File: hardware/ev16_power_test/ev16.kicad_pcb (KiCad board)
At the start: 4 copper layers, 125 x 80 mm, 172 parts, among them CN1 Conn_05x02_Female, CN2 PJ-242, J1 USB_C_Receptacle, J10 Conn_01x03_Pin, J11 Conn_02x05_Counter_Clockwise, J2 Conn_01x02_Socket, J3 AudioJack4, J4 Conn_02x03_Odd_Even, J5 Conn_02x03_Odd_Even, J6 Conn_02x05_Counter_Clockwise, J7 Conn_02x05_Counter_Clockwise, J8 Conn_02x05_Counter_Clockwise, J9 Conn_02x05_Counter_Clockwise, Q1 2N7002, Q2 2N7002, Q3 2N7002, SW1 SW_SPDT, SW2 SW_Push, SW3 SW_Push, SW4 SW_Push, SW5 SW_Push, SW6 SW_Push, SW7 SW_Push, U1 BQ21040DBV, U10 STM32F405RGTx, U2 USBLC6-2P6, U3 STM32F072CBTx, U4 CH340C, U5 TPS63060, U6 WM8960CGEFL/RV, U7 ESP32-S3-WROOM-1, U8 M24C02-RMN6TP, Y1 Crystal_GND24

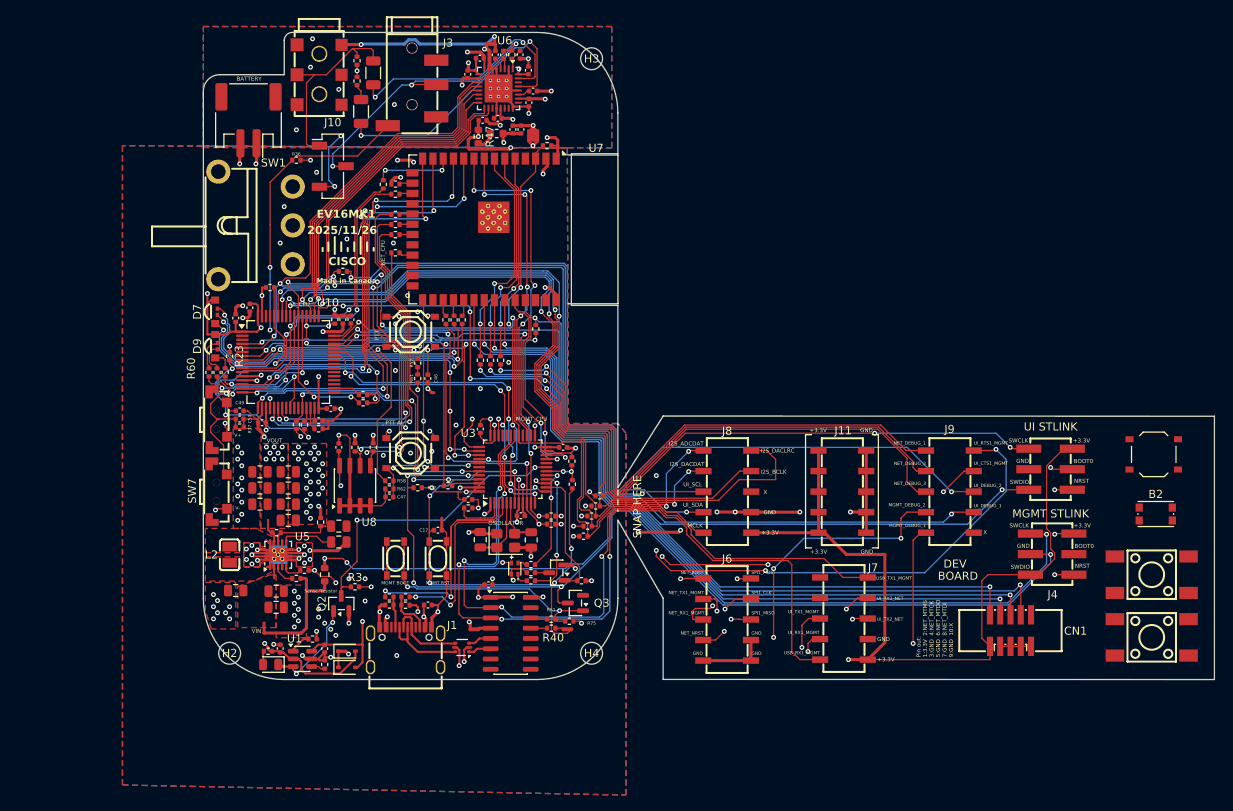
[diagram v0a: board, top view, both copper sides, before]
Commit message: New linear regulator, ideal diodes, began working on the layout
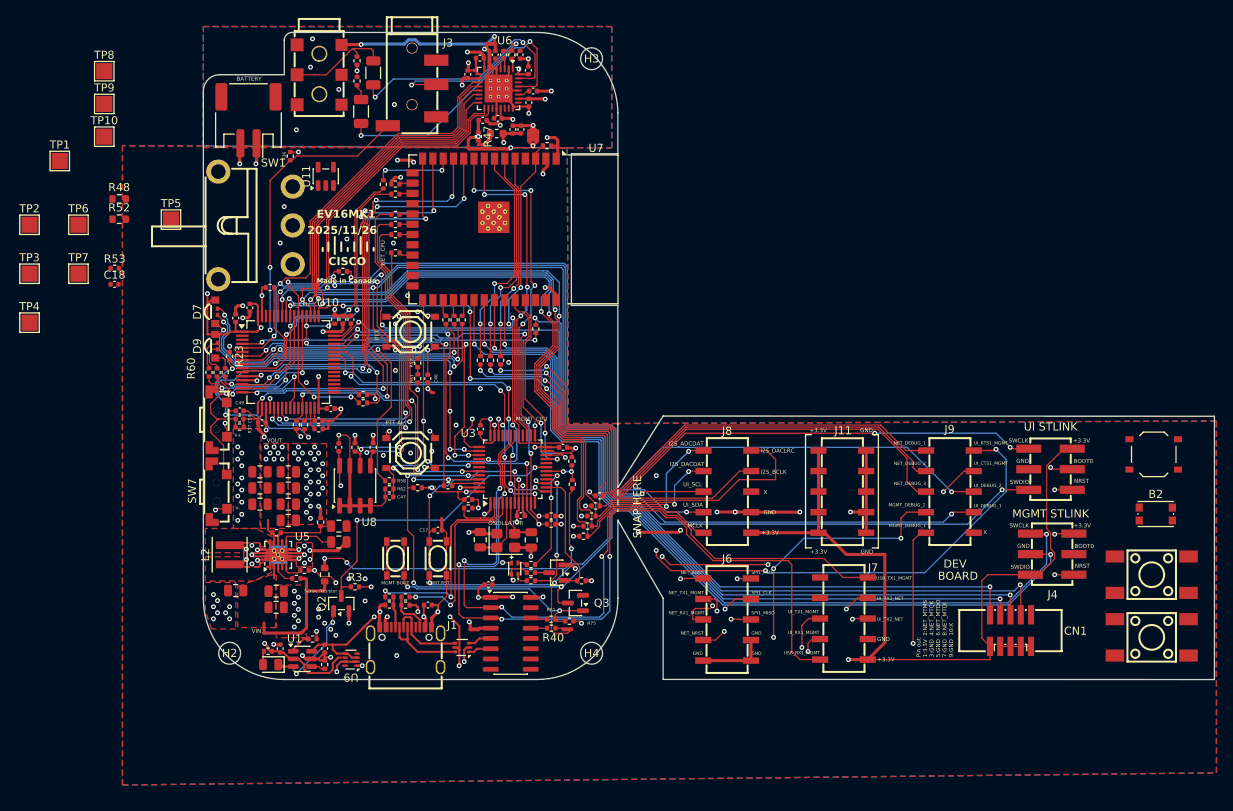
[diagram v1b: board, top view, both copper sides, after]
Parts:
- removed D2, D3: 1N5819WS, Diode_SMD:D_SOD-323
- removed J10: Conn_01x03_Pin, Connector_PinSocket_2.54mm:PinSocket_1x03_P2.54mm_Vertical_SMD_Pin1Left
- added C18: 1u, Capacitor_SMD:C_0402_1005Metric, F.Cu at (39.0, 61.1)
- added R48: 0R1, Resistor_SMD:R_0603_1608Metric, F.Cu at (39.6, 50.6)
- added R52: 0R1, Resistor_SMD:R_0603_1608Metric, F.Cu at (39.6, 53.1)
- added R53: 15k, Resistor_SMD:R_0402_1005Metric, F.Cu at (39.0, 59.2)
- added TP1: TestPoint, TestPoint:TestPoint_Pad_2.0x2.0mm, F.Cu at (32.2, 45.9)
- added TP10: TestPoint, TestPoint:TestPoint_Pad_2.0x2.0mm, F.Cu at (37.8, 42.9)
- added TP2: TestPoint, TestPoint:TestPoint_Pad_2.0x2.0mm, F.Cu at (28.5, 53.8)
- added TP3: TestPoint, TestPoint:TestPoint_Pad_2.0x2.0mm, F.Cu at (28.5, 59.8)
- added TP4: TestPoint, TestPoint:TestPoint_Pad_2.0x2.0mm, F.Cu at (28.5, 65.9)
- added TP5: TestPoint, TestPoint:TestPoint_Pad_2.0x2.0mm, F.Cu at (46.0, 53.1)
- added TP6: TestPoint, TestPoint:TestPoint_Pad_2.0x2.0mm, F.Cu at (34.6, 53.8)
- added TP7: TestPoint, TestPoint:TestPoint_Pad_2.0x2.0mm, F.Cu at (34.6, 59.8)
- added TP8: TestPoint, TestPoint:TestPoint_Pad_2.0x2.0mm, F.Cu at (37.8, 34.8)
- added TP9: TestPoint, TestPoint:TestPoint_Pad_2.0x2.0mm, F.Cu at (37.8, 38.8)
- added U11: ME6211C28M5, Package_TO_SOT_SMD:SOT-23-5, F.Cu at (65.1, 47.8)
- added U9: TPS2116DRL, Package_TO_SOT_SMD:SOT-583-8, F.Cu at (68.3, 107.5)
- L2: value 1uH -> 1.5uH; footprint Hactar_Footprints:MCL2016A1R0MT -> Inductor_SMD:L_Coilcraft_XxL4020
- R47: value 0R1 -> 10k; footprint Resistor_SMD:R_0603_1608Metric -> Resistor_SMD:R_0402_1005Metric
- moved R36 0.90 mm to (60.8, 45.3), turned to 90 degrees
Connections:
- C10 pad 1: +3.3VA -> Net-(C10-Pad1)
- C11 pad 1: +3.3VA -> Net-(C10-Pad1)
- C22 pad 1: +3.3V -> Net-(U5-VOUT)
- C24 pad 1: +3.3V -> Net-(U5-VOUT)
- C27 pad 1: +3.3V -> Net-(U5-VOUT)
- C29 pad 1: +3.3V -> Net-(U5-VOUT)
- C30 pad 1: +3.3V -> Net-(U5-VOUT)
- C31 pad 1: +3.3V -> Net-(U5-VOUT)
- C35 pad 1: +3.3V -> Net-(U5-VOUT)
- L1 pad 1: Net-(L1-Pad1) -> Net-(U11-V_{OUT})
- L1 pad 2: +3.3VA -> Net-(C10-Pad1)
- R12 pad 2: Net-(SW1-C) -> VSYS
- R14 pad 1: Net-(SW1-C) -> VSYS
- R26 pad 2: +3.3V -> Net-(U5-VOUT)
- R28 pad 2: +3.3V -> Net-(U5-VOUT)
- R47 pad 1: +3.3V -> GND
- R47 pad 2: Net-(L1-Pad1) -> Net-(U9-PR1)
- SW1 pad 2: Net-(D2-K) -> VSYS
- U5 pad 9: +3.3V -> Net-(U5-VOUT)
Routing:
- net VSYS: track 0.00 -> 102.3 mm, vias 0 -> 3
- net Net-(D2-K): track 64.7 -> 0.00 mm, vias 1 -> 0
- net Net-(SW1-C): track 94.2 -> 73.5 mm, vias 3 -> 1
- net /MIC_P: track 36.2 -> 19.7 mm, vias 3 -> 2
- net /HP_L: track 23.8 -> 13.1 mm
- net GNDA: track 86.0 -> 76.9 mm, vias 13 -> 11
- net +3.3V: track 296.4 -> 287.9 mm, vias 47 -> 37
- net Net-(U5-VOUT): track 0.00 -> 7.36 mm, vias 0 -> 10
- net VBUS: track 37.8 -> 34.5 mm, vias 4 -> 5
- net Net-(U11-V_{OUT}): track 0.00 -> 2.39 mm
- net Net-(L1-Pad1): track 2.39 -> 0.00 mm
- net Net-(J2-Pin_2): track 79.5 -> 77.6 mm
- net GND: track 312.3 -> 313.0 mm
- added copper zone on F.Cu, net Net-(U5-VOUT)
- removed copper zone on F.Cu, net +3.3V

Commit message: finished laying out the board with the power changes
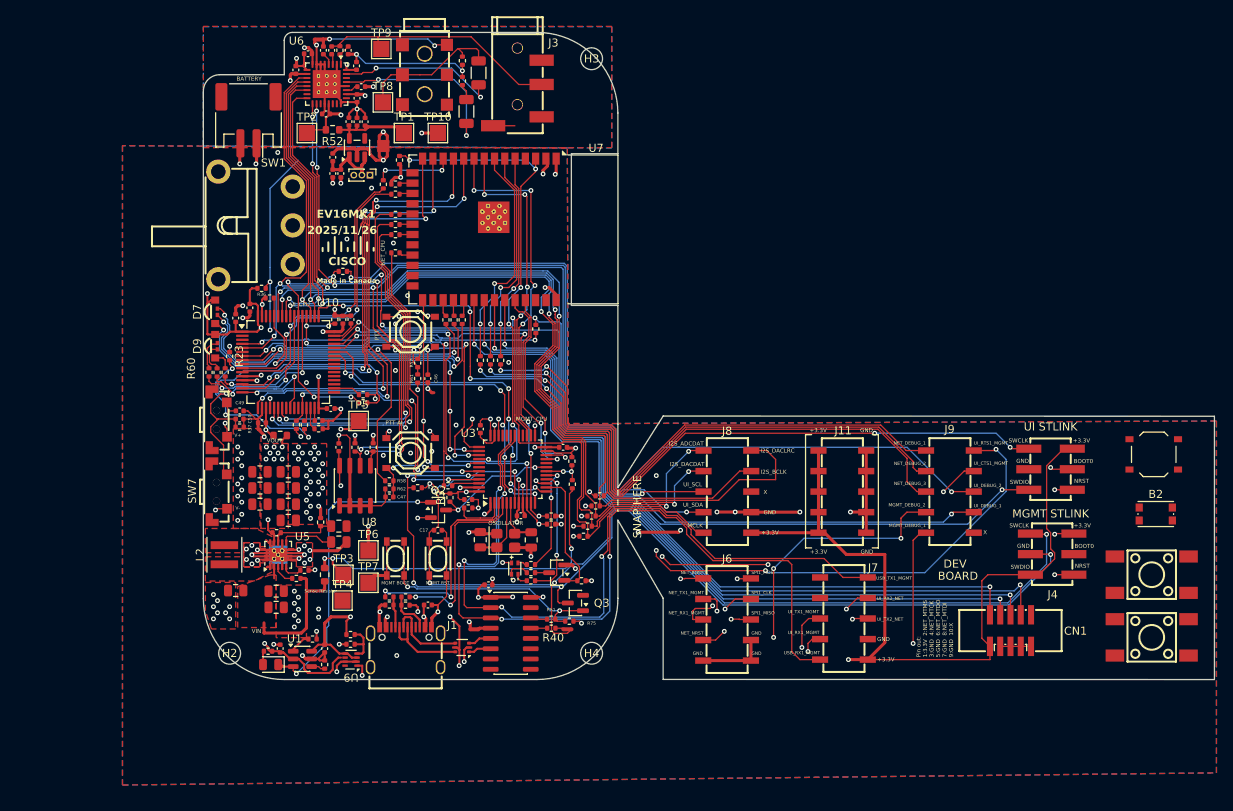
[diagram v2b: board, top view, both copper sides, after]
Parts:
- removed L1: 120Ω, Inductor_SMD:L_0603_1608Metric
- added C51: 100n, Capacitor_SMD:C_0402_1005Metric, F.Cu at (66.0, 47.4)
- added C52: 100n, Capacitor_SMD:C_0402_1005Metric, F.Cu at (66.0, 45.4)
- added J10: Conn_01x03_Pin, Connector_PinHeader_1.00mm:PinHeader_1x03_P1.00mm_Vertical, F.Cu at (70.6, 47.6)
- C10: value 1u -> 100n
- C11: value 10n -> 100n
- C24, C27, C29, C30, C31, C35: value 10u -> 22u
- moved R47 64.7 mm to (68.2, 105.6), turned to 0 degrees
- moved TP6 53.9 mm to (70.4, 94.0)
- moved R53 53.9 mm to (68.2, 104.4), turned to 180 degrees
- moved TP3 53.8 mm to (67.3, 97.1)
- moved TP7 52.4 mm to (70.4, 98.0)
- moved TP4 51.7 mm to (67.2, 100.2)
- moved TP1 42.7 mm to (74.8, 42.4)
- moved TP10 41.3 mm to (79.0, 42.4)
- moved TP2 36.1 mm to (62.8, 42.4)
- moved R48 35.4 mm to (59.5, 79.8), turned to 180 degrees
- moved C18 35.3 mm to (68.0, 41.0), turned to 90 degrees
- moved TP9 34.9 mm to (72.0, 32.0)
- moved TP8 34.7 mm to (72.2, 38.6)
- moved TP5 34.0 mm to (69.2, 78.0)
- moved R52 28.6 mm to (66.0, 42.0), turned to 180 degrees
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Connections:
- C10 pad 1: Net-(C10-Pad1) -> Net-(U11-V_{OUT})
- C11 pad 1: Net-(C10-Pad1) -> Net-(U11-V_{OUT})
- C18 pad 2: GND -> GNDA
- C7 pad 1: +3.3V -> Net-(J10-Pin_2)
- R52 pad 1: Net-(C10-Pad1) -> Net-(U11-V_{OUT})
- TP1 pad 1: Net-(C10-Pad1) -> Net-(U11-V_{OUT})
- U10 pad 13: +3.3VA -> +3.3V
- U11 pad 1: +3.3V -> Net-(J10-Pin_2)
- U11 pad 3: +3.3V -> Net-(J10-Pin_2)
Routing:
- net +3.3VA: track 80.6 -> 21.9 mm, vias 5 -> 3
- net GNDA: track 76.9 -> 103.5 mm, vias 11 -> 7
- net Net-(D1-K): track 12.7 -> 38.0 mm
- net /CHG_FB: track 37.6 -> 16.0 mm
- net Net-(U5-VOUT): track 7.36 -> 26.1 mm, vias 10 -> 11
- net /NET_NRST: track 97.6 -> 113.1 mm, vias 5 -> 7
- net VSYS: track 102.3 -> 117.0 mm
- net Net-(U6-HP_R): track 35.3 -> 22.5 mm
- net /UI_SDA1: track 153.0 -> 141.3 mm, vias 6 -> 8
- net /UI_SCL1: track 147.8 -> 136.5 mm, vias 6 -> 8
- net /MIC_P: track 19.7 -> 30.7 mm, vias 2 -> 0
- net /I2S_BCLK: track 130.2 -> 119.7 mm
- net Net-(U6-HP_L): track 30.4 -> 20.0 mm
- net GND: track 313.0 -> 302.8 mm, vias 144 -> 137
- net /MCLK: track 143.1 -> 133.0 mm
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- added copper zone on In2.Cu, net +3.3VA
- removed copper zone on B.Cu, net GNDA
- removed copper zone on F.Cu, net GNDA
- removed copper zone on In2.Cu, net GNDA

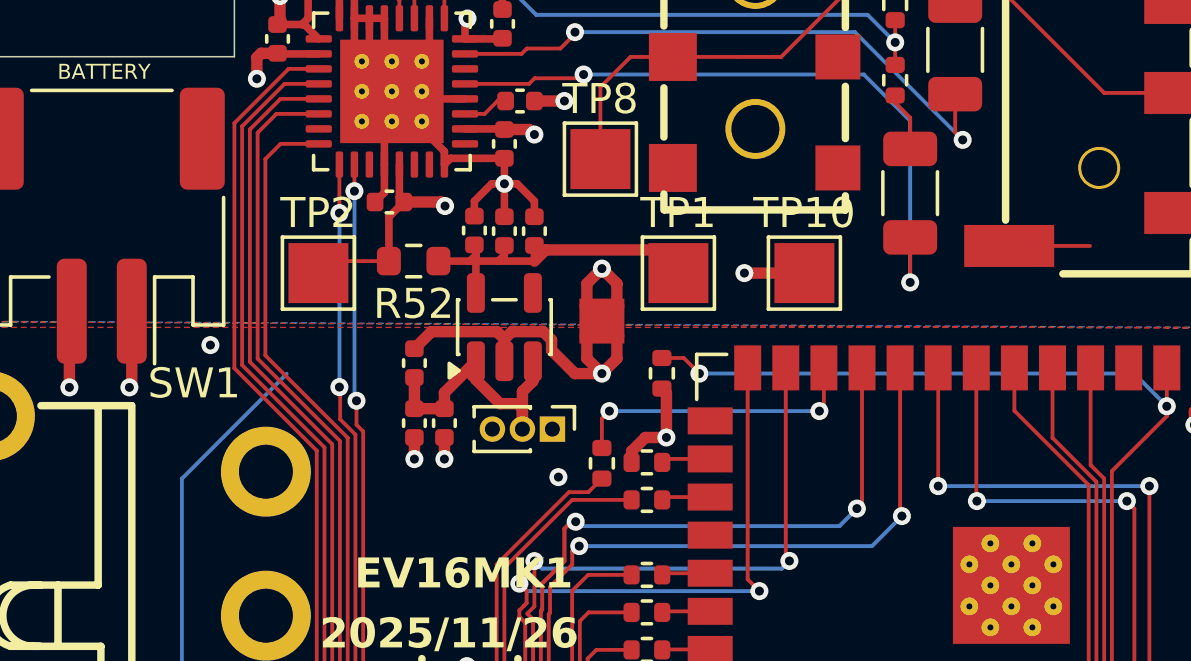
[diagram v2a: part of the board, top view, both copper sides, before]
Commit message: Removed extra caps from linear power supply that wasn't needed
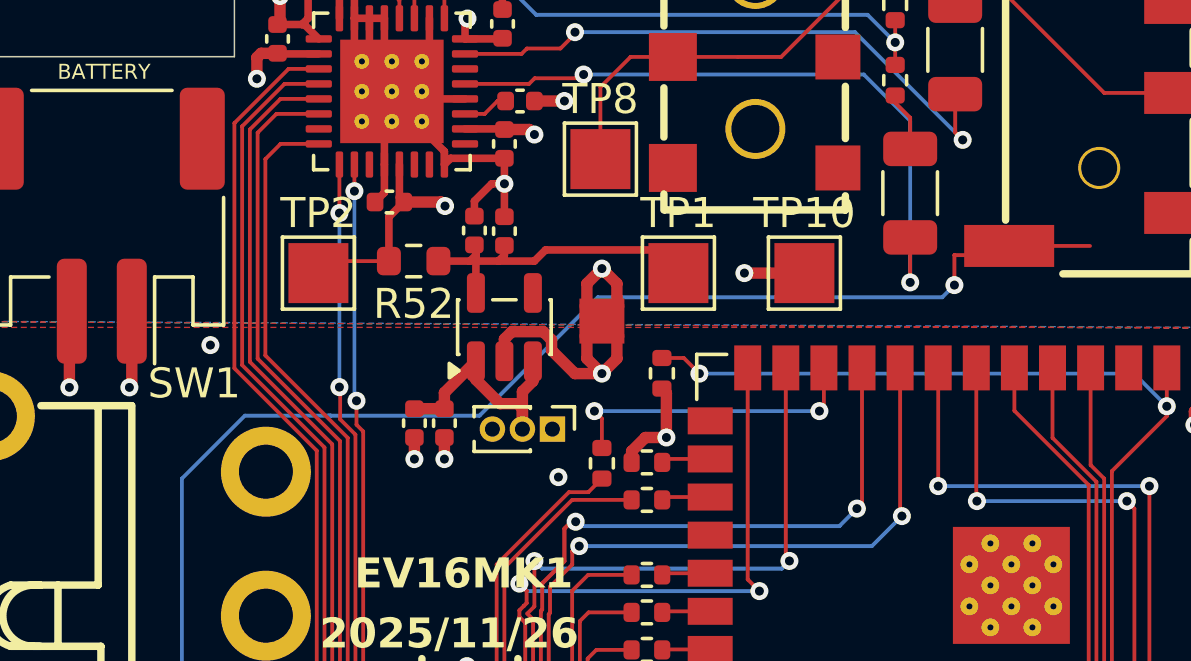
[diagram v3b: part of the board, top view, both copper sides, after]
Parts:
- removed C11, C52: 100n, Capacitor_SMD:C_0402_1005Metric
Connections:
- U11 pad 2: GND -> GNDA
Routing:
- net /MIC_IO: track 36.9 -> 63.4 mm, vias 3 -> 4
- net GND: track 302.8 -> 299.5 mm
- net GNDA: track 103.5 -> 101.7 mm
- net Net-(J10-Pin_2): track 9.52 -> 8.48 mm
- net Net-(U11-V_{OUT}): track 11.3 -> 10.8 mm
- net /NET_READY: track 9.84 -> 10.3 mm
- added copper zone on F.Cu, net GNDA
